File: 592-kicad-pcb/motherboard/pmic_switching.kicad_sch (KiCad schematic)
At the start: 5 parts

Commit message: current monitor symbol
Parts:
- removed ISL54059IRUZ-T_uTQFN1, ISL54059IRUZ-T_uTQFN2: ~, symbol 592-partslib:ISL54059IRUZ-T_uTQFN
- added U16: INA138NA/3K, symbol 592-partslib:INA138NA/3K
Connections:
- net VCCD: now also ISL54059IRUZ-T_uTQFN3.9 (COM1)
- net VDDA, VDDIO: now also ISL54059IRUZ-T_uTQFN3.4 (COM2)
- net VDD_EXT: now also ISL54059IRUZ-T_uTQFN5.9 (COM1)
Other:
- moved on the sheet: ISL54059IRUZ-T_uTQFN3, ISL54059IRUZ-T_uTQFN5
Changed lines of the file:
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@@
 		(rev "0.00")
 	)
-	(text_box "1V8 USER DIGITAL"
-		(exclude_from_sim no)
-		(at 46.99 87.63 0)
-		(size 181.61 31.75)
+	(text_box "1V8 USER DIGITAL\n3V3 USER ANALOG"
+		(exclude_from_sim no)
+		(at 46.99 66.04 0)
+		(size 168.91 35.56)
 		(margins 0.9525 0.9525 0.9525 0.9525)
 		(stroke
@@
 		)
 	)
-	(text_box "3V3 USER ANALOG"
-		(exclude_from_sim no)
-		(at 46.99 158.75 0)
-		(size 113.03 31.75)
+	(text_box "3V3 MGMT\n1V8 MGMT"
+		(exclude_from_sim no)
+		(at 46.99 16.51 0)
+		(size 92.71 44.45)
 		(margins 0.9525 0.9525 0.9525 0.9525)
 		(stroke
@@
 		)
 	)
-	(text_box "3V3 MGMT"
-		(exclude_from_sim no)
-		(at 46.99 16.51 0)
-		(size 113.03 31.75)
-		(margins 0.9525 0.9525 0.9525 0.9525)
-		(stroke
-			(width 0)
-			(type solid)
-		)
-		(fill
-			(type none)
-		)
-		(effects
-			(font
-				(size 1.27 1.27)
-			)
-			(justify left top)
-		)
-	)
 	(text_box "CURRENT MONITOR"
 		(exclude_from_sim no)
-		(at 177.8 88.9 0)
-		(size 49.53 25.4)
+		(at 176.53 68.58 0)
+		(size 36.83 25.4)
 		(margins 0.9525 0.9525 0.9525 0.9525)
 		(stroke
@@
 		)
 	)
-	(text_box "1V8 MGMT"
-		(exclude_from_sim no)
-		(at 46.99 52.07 0)
-		(size 113.03 31.75)
-		(margins 0.9525 0.9525 0.9525 0.9525)
-		(stroke
-			(width 0)
-			(type solid)
-		)
-		(fill
-			(type none)
-		)
-		(effects
-			(font
-				(size 1.27 1.27)
-			)
-			(justify left top)
-		)
-	)
 	(wire
 		(pts
@@
 	(wire
 		(pts
-			(xy 152.4 63.5) (xy 165.1 63.5)
+			(xy 91.44 38.1) (xy 88.9 38.1)
 		)
 		(stroke
@@
 	(wire
 		(pts
-			(xy 222.25 101.6) (xy 232.41 101.6)
+			(xy 210.82 81.28) (xy 218.44 81.28)
 		)
 		(stroke
@@
 	(wire
 		(pts
-			(xy 152.4 25.4) (xy 165.1 25.4)
+			(xy 116.84 38.1) (xy 119.38 38.1)
 		)
 		(stroke
@@
 	(wire
 		(pts
-			(xy 222.25 116.84) (xy 232.41 116.84)
+			(xy 222.25 95.25) (xy 232.41 95.25)
 		)
 		(stroke
@@
 	(wire
 		(pts
-			(xy 154.94 171.45) (xy 166.37 171.45)
+			(xy 91.44 83.82) (xy 88.9 83.82)
 		)
 		(stroke
@@
 	)
 	(label "dig_to_adc"
-		(at 232.41 101.6 0)
+		(at 218.44 81.28 0)
 		(effects
 			(font
@@
 	)
 	(label "VCCD"
-		(at 165.1 63.5 0)
+		(at 88.9 38.1 180)
+		(effects
+			(font
+				(size 1.27 1.27)
+			)
+			(justify right bottom)
+		)
+	)
+	(label "VDDA, VDDIO"
+		(at 119.38 38.1 0)
 		(effects
 			(font
@@
 		)
 	)
-	(label "VDDA, VDDIO"
-		(at 165.1 25.4 0)
-		(effects
-			(font
-				(size 1.27 1.27)
-			)
-			(justify left bottom)
-		)
-	)
 	(label "VCCD1, VCCD2"
-		(at 232.41 116.84 0)
+		(at 232.41 95.25 0)
 		(effects
 			(font
@@
 	)
 	(label "VDD_EXT"
-		(at 166.37 171.45 0)
-		(effects
-			(font
-				(size 1.27 1.27)
-			)
-			(justify left bottom)
+		(at 88.9 83.82 180)
+		(effects
+			(font
+				(size 1.27 1.27)
+			)
+			(justify right bottom)
 		)
 	)
@@
 	(symbol
 		(lib_id "592-partslib:ISL54059IRUZ-T_uTQFN")
-		(at 77.47 175.26 0)
+		(at 104.14 83.82 0)
 		(unit 1)
 		(exclude_from_sim no)
@@
 		(dnp no)
 		(property "Reference" "ISL54059IRUZ-T_uTQFN5"
-			(at 65.786 171.958 0)
+			(at 92.456 80.518 0)
 			(effects
 				(font
@@
 		)
 		(property "Value" "~"
-			(at 64.77 171.958 0)
+			(at 91.44 80.518 0)
 			(effects
 				(font
@@
 		)
 		(property "Footprint" ""
-			(at 77.47 175.26 0)
+			(at 104.14 83.82 0)
 			(effects
 				(font
@@
 		)
 		(property "Datasheet" ""
-			(at 77.47 175.26 0)
+			(at 104.14 83.82 0)
 			(effects
 				(font
@@
 		)
 		(property "Description" ""
-			(at 77.47 175.26 0)
+			(at 104.14 83.82 0)
 			(effects
 				(font
@@
 	)
 	(symbol
-		(lib_id "592-partslib:ISL54059IRUZ-T_uTQFN")
-		(at 77.47 67.31 0)
+		(lib_id "592-partslib:INA138NA/3K")
+		(at 193.04 81.28 0)
 		(unit 1)
 		(exclude_from_sim no)
@@
 		(on_board yes)
 		(dnp no)
-		(property "Reference" "ISL54059IRUZ-T_uTQFN1"
-			(at 65.786 64.008 0)
-			(effects
-				(font
-					(size 1.27 1.27)
-				)
-				(justify left)
-			)
-		)
-		(property "Value" "~"
-			(at 64.77 64.008 0)
-			(effects
-				(font
-					(size 1.27 1.27)
-				)
-				(justify left)
+		(property "Reference" "U16"
+			(at 193.294 80.518 0)
+			(effects
+				(font
+					(size 1.27 1.27)
+				)
+			)
+		)
+		(property "Value" "INA138NA/3K"
+			(at 193.548 82.296 0)
+			(effects
+				(font
+					(size 1.27 1.27)
+				)
 			)
 		)
 		(property "Footprint" ""
-			(at 77.47 67.31 0)
-			(effects
-				(font
-					(size 1.27 1.27)
-				)
-				(hide yes)
-			)
-		)
-		(property "Datasheet" ""
-			(at 77.47 67.31 0)
-			(effects
-				(font
-					(size 1.27 1.27)
-				)
-				(hide yes)
-			)
-		)
-		(property "Description" ""
-			(at 77.47 67.31 0)
+			(at 193.04 81.28 0)
+			(effects
+				(font
+					(size 1.27 1.27)
+				)
+				(hide yes)
+			)
+		)
+		(property "Datasheet" "https://www.lcsc.com/datasheet/C47914.pdf"
+			(at 193.04 81.28 0)
+			(effects
+				(font
+					(size 1.27 1.27)
+				)
+				(hide yes)
+			)
+		)
+		(property "Description" "TI current monitor"
+			(at 193.04 81.28 0)
 			(effects
 				(font
@@
 		(pin "5"
 		)
+		(pin "3"
+		)
 		(pin "4"
 		)
-		(pin "8"
-		)
-		(pin "3"
-		)
-		(pin "9"
-		)
-		(pin "7"
-		)
 		(pin "1"
 		)
-		(pin "2"
-		)
-		(pin "6"
-		)
-		(pin "10"
+		(pin "GND"
 		)
 		(instances
 			(project ""
 				(path "/5b0c97ac-fa03-4db8-b41b-0eee32b6f55d/f049e4ad-bebe-4338-850a-2727de737ae9/260af3dc-9286-4c76-9c6c-eeb806d3e6e5"
-					(reference "ISL54059IRUZ-T_uTQFN1")
+					(reference "U16")
 					(unit 1)
 				)
@@
 	(symbol
 		(lib_id "592-partslib:ISL54059IRUZ-T_uTQFN")
-		(at 77.47 31.75 0)
-		(unit 1)
-		(exclude_from_sim no)
-		(in_bom yes)
-		(on_board yes)
-		(dnp no)
-		(property "Reference" "ISL54059IRUZ-T_uTQFN2"
-			(at 65.786 28.448 0)
-			(effects
-				(font
-					(size 1.27 1.27)
-				)
-				(justify left)
-			)
-		)
-		(property "Value" "~"
-			(at 64.77 28.448 0)
-			(effects
-				(font
-					(size 1.27 1.27)
-				)
-				(justify left)
-			)
-		)
-		(property "Footprint" ""
-			(at 77.47 31.75 0)
-			(effects
-				(font
-					(size 1.27 1.27)
-				)
-				(hide yes)
-			)
-		)
-		(property "Datasheet" ""
-			(at 77.47 31.75 0)
-			(effects
-				(font
-					(size 1.27 1.27)
-				)
-				(hide yes)
-			)
-		)
-		(property "Description" ""
-			(at 77.47 31.75 0)
-			(effects
-				(font
-					(size 1.27 1.27)
-				)
-				(hide yes)
-			)
-		)
-		(pin "5"
-		)
-		(pin "4"
-		)
-		(pin "8"
-		)
-		(pin "3"
-		)
-		(pin "9"
-		)
-		(pin "7"
-		)
-		(pin "1"
-		)
-		(pin "2"
-		)
-		(pin "6"
-		)
-		(pin "10"
-		)
-		(instances
-			(project "motherboard"
-				(path "/5b0c97ac-fa03-4db8-b41b-0eee32b6f55d/f049e4ad-bebe-4338-850a-2727de737ae9/260af3dc-9286-4c76-9c6c-eeb806d3e6e5"
-					(reference "ISL54059IRUZ-T_uTQFN2")
-					(unit 1)
-				)
-			)
-		)
-	)
-	(symbol
-		(lib_id "592-partslib:ISL54059IRUZ-T_uTQFN")
-		(at 77.47 104.14 0)
+		(at 104.14 38.1 0)
 		(unit 1)
 		(exclude_from_sim no)
@@
 		(dnp no)
 		(property "Reference" "ISL54059IRUZ-T_uTQFN3"
-			(at 65.786 100.838 0)
+			(at 92.456 34.798 0)
 			(effects
 				(font
@@
 		)
 		(property "Value" "~"
-			(at 64.77 100.838 0)
+			(at 91.44 34.798 0)
 			(effects
 				(font
@@
 		)
 		(property "Footprint" ""
-			(at 77.47 104.14 0)
+			(at 104.14 38.1 0)
 			(effects
 				(font
@@
 		)
 		(property "Datasheet" ""
-			(at 77.47 104.14 0)
+			(at 104.14 38.1 0)
 			(effects
 				(font
@@
 		)
 		(property "Description" ""
-			(at 77.47 104.14 0)
-			(effects
-				(font
+			(at 104.14 38.1 0)
+			(effects
+				(font

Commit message: working through switching
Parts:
- removed ISL54059IRUZ-T_uTQFN3, ISL54059IRUZ-T_uTQFN4, ISL54059IRUZ-T_uTQFN5: ~, symbol 592-partslib:ISL54059IRUZ-T_uTQFN
- added R54, R55: R_Small, symbol Device:R_Small
- added U17: ~, symbol 592-partslib:INA138NA/3K
- added U18, U19, U20: ~, uTQFN, symbol 592-partslib:ISL54059IRUZ-T_uTQFN
- U16: value INA138NA/3K -> ~
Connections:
- net VCCD: now also U20.9 (COM1)
- net VCCD1, VCCD2: now also U16.4 (VIN-), R54.2
- net VDDA, VDDIO: now also U20.4 (COM2)
- net VDD_EXT: now also R55.2, U17.4 (VIN-)
- net dig_to_adc: now also U16.1 (OUT)
- net gpio_0: now also U20.7 (IN1)
- net gpio_1: now also U20.6 (IN2)
- net gpio_2: now also U18.7 (IN1)
- net gpio_3: now also U18.6 (IN2)
- net gpio_4: now also U19.7 (IN1)
- net ldo_to_adc: now also U17.1 (OUT)
- net at U16.3 (VIN+): now also R54.1, U18.9 (COM1)
- net at U16.5 (V+): now also U18.2 (V+)
- new net: R55.1, U17.3 (VIN+), U19.9 (COM1)
- new net: U17.5 (V+), U19.2 (V+)
- new net GND: U16.2 (GND), U17.2 (GND), U18.1 (GND), U19.1 (GND), U19.4 (COM2), U20.1 (GND)
- new net gpio_5: U19.6 (IN2)

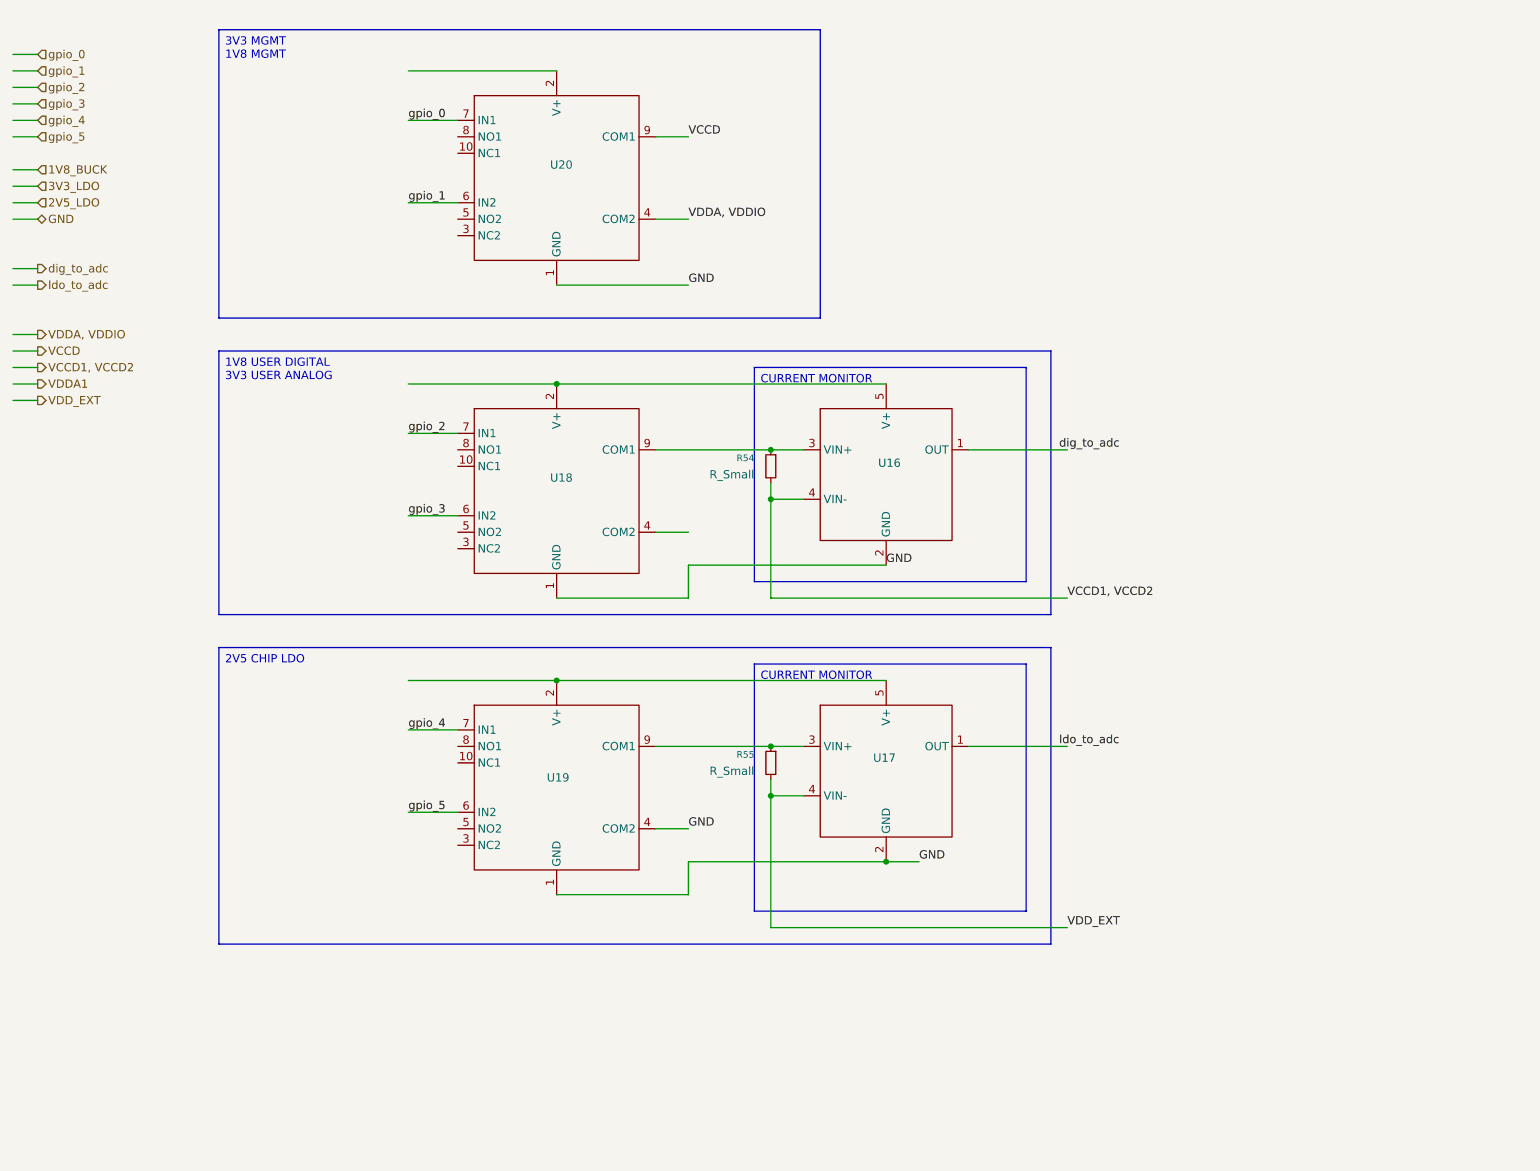
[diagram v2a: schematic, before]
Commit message: pmic switching schem done
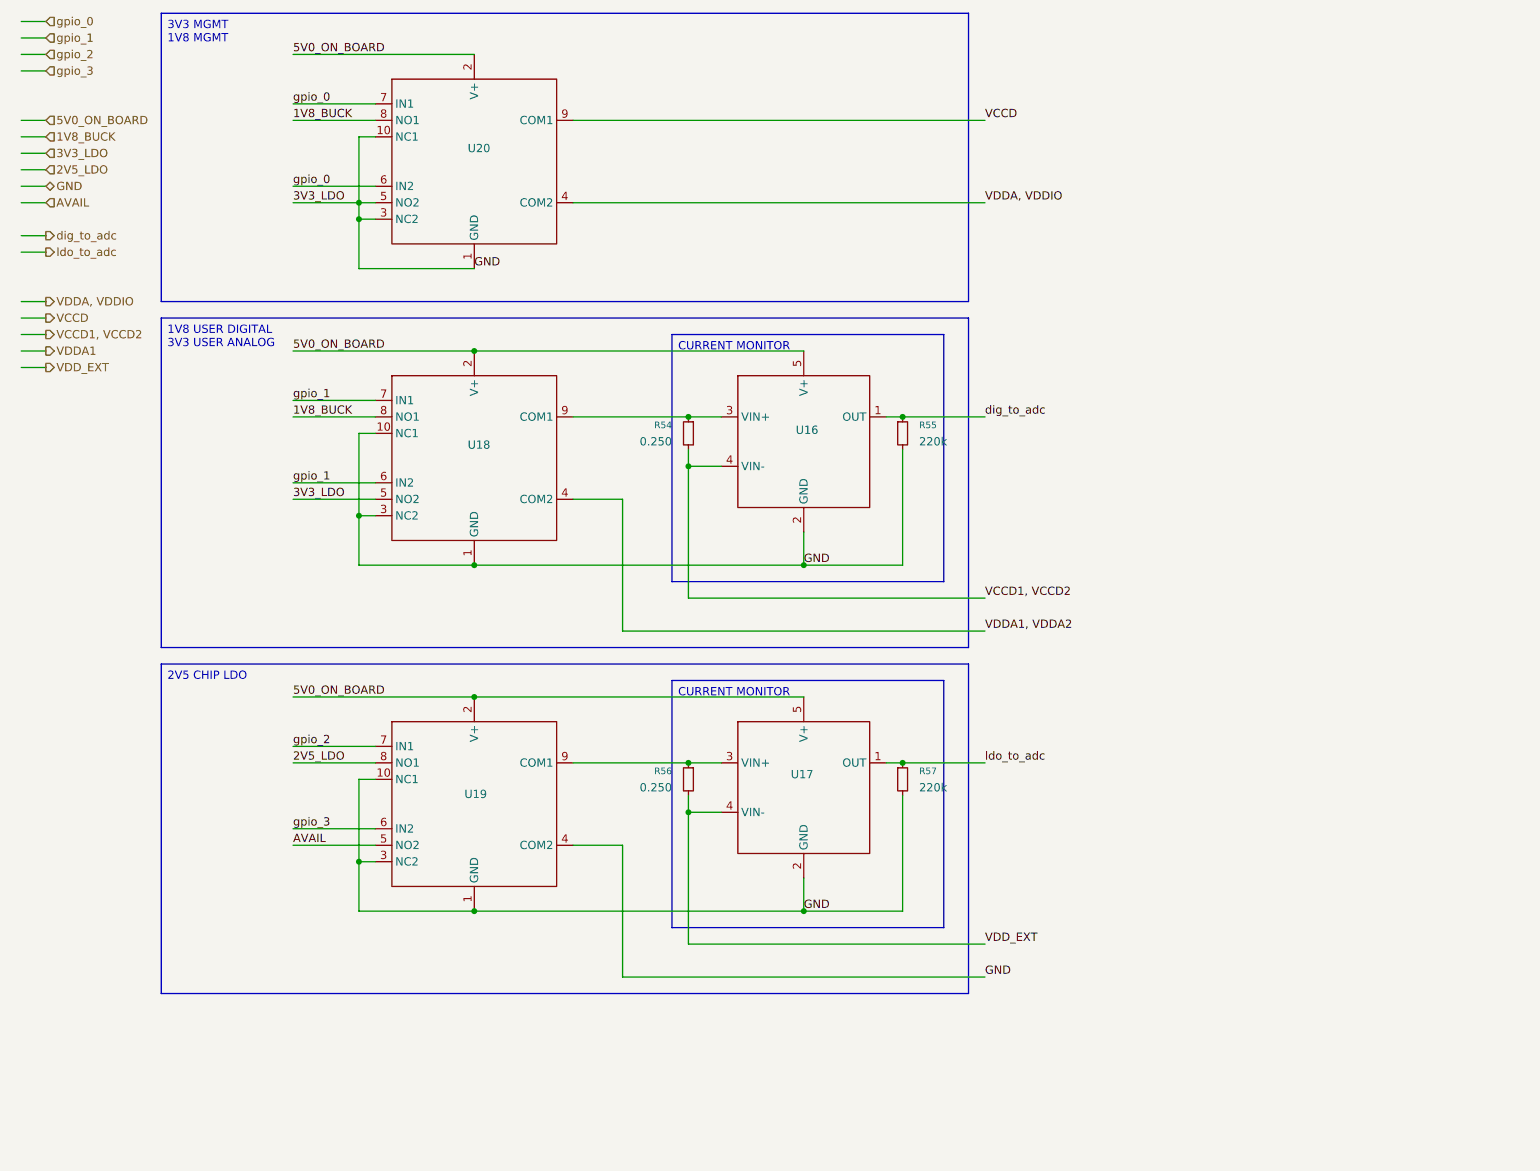
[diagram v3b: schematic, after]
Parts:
- added R55, R57: 220k, symbol Device:R_Small
- R54: value R_Small -> 0.250
- R56: renamed from R55; value R_Small -> 0.250
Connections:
- net GND is gone; now on net 3V3_LDO: U16.2 (GND), U17.2 (GND), U18.1 (GND), U19.1 (GND), U19.4 (COM2), U20.1 (GND)
- net gpio_4 is gone; now on net gpio_2: U19.7 (IN1)
- net gpio_5 is gone; now on net gpio_3: U19.6 (IN2)
- net 1V8_BUCK: now also U18.8 (NO1), U20.8 (NO1)
- net 2V5_LDO: now also U19.8 (NO1)
- net 3V3_LDO: now also U18.10 (NC1), U18.3 (NC2), U18.5 (NO2), U19.10 (NC1), U19.3 (NC2), U20.10 (NC1), U20.3 (NC2), U20.5 (NO2), R55.2, R57.2
- net dig_to_adc: now also R55.1
- net gpio_0: now also U20.6 (IN2)
- net gpio_1: now also U18.6 (IN2), U18.7 (IN1); no longer U20.6 (IN2)
- net gpio_2: no longer U18.7 (IN1)
- net gpio_3: no longer U18.6 (IN2)
- net ldo_to_adc: now also R57.1
- net 5V0_ON_BOARD: now reaches U17.5 (V+), U19.2 (V+)
- net 5V0_ON_BOARD: now also U16.5 (V+), U18.2 (V+), U20.2 (V+)
- net AVAIL: now reaches U19.5 (NO2)
- net VDDA1, VDDA2: now reaches U18.4 (COM2)
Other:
- moved on the sheet: R54, R56, U16, U17, U18, U19, U20

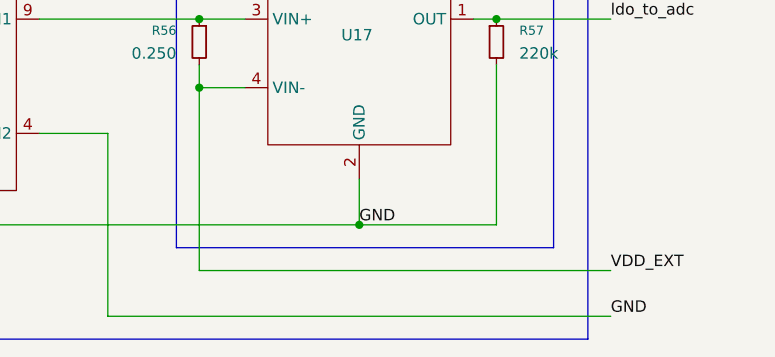
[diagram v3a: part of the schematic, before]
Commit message: fuses, ferrite bead, 5V0 selection connector
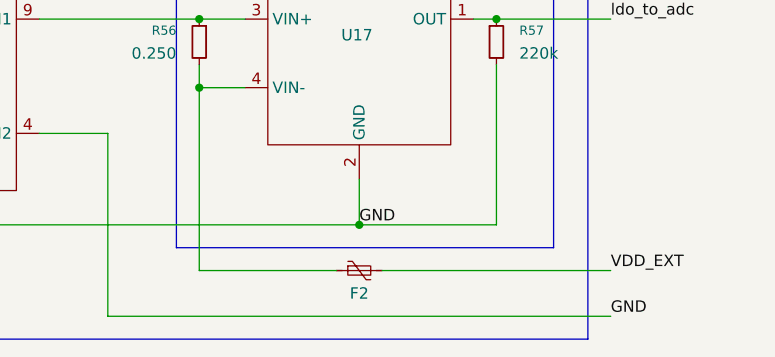
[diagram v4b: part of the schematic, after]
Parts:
- added F2: (no value), 0603, symbol Device:Polyfuse_Small
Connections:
- net VDD_EXT: now also F2.2; no longer R56.2, U17.4 (VIN-)
- new net: F2.1, R56.2, U17.4 (VIN-)
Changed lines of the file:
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@@
 	(wire
 		(pts
-			(xy 119.38 157.48) (xy 165.1 157.48)
+			(xy 119.38 157.48) (xy 134.62 157.48)
 		)
 		(stroke
@@
 		(pts
 			(xy 16.51 17.78) (xy 20.32 17.78)
+		)
+		(stroke
+			(width 0)
+			(type default)
+		)
+	)
+	(wire
+		(pts
+			(xy 139.7 157.48) (xy 165.1 157.48)
 		)
 		(stroke
@@
 					(unit 1)
 				)
+			)
+		)
+	)
+	(symbol
+		(lib_id "Device:Polyfuse_Small")
+		(at 137.16 157.48 90)
+		(mirror x)
+		(unit 1)
+		(exclude_from_sim no)
+		(in_bom yes)
+		(on_board yes)
+		(dnp no)
+		(property "Reference" "F2"
+			(at 137.16 160.02 90)
+			(effects
+				(font
+					(size 1.27 1.27)
+				)
+			)
+		)
+		(property "Value" ""
+			(at 137.16 159.258 90)
+			(effects
+				(font
+					(size 1.27 1.27)
+				)
+			)
+		)
+		(property "Footprint" "0603"
+			(at 142.24 158.75 0)
+			(effects
+				(font
+					(size 1.27 1.27)
+				)
+				(justify left)
+				(hide yes)
+			)
+		)
+		(property "Datasheet" "https://www.lcsc.com/datasheet/C224188.pdf"
+			(at 137.16 157.48 0)
+			(effects
+				(font
+					(size 1.27 1.27)
+				)
+				(hide yes)
+			)
+		)
+		(property "Description" "Resettable fuse, polymeric positive temperature coefficient, small symbol"
+			(at 137.16 157.48 0)
+			(effects
+				(font
+					(size 1.27 1.27)
+				)
+				(hide yes)
+			)
+		)
+		(pin "1"
+		)
+		(pin "2"
+		)
+		(instances
+			(project "motherboard"
+				(path "/5b0c97ac-fa03-4db8-b41b-0eee32b6f55d/f049e4ad-bebe-4338-850a-2727de737ae9/260af3dc-9286-4c76-9c6c-eeb806d3e6e5"
+					(reference "F2")
+					(unit 1)
+				)
